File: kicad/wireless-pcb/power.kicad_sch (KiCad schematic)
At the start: 16 parts, among them J2 Conn_01x02_Socket, J4 Conn_01x02_Socket, Q1 AO3401A, U1 XC6206PxxxMR-Regulator_Linear, U8 MCP73832-2-OT

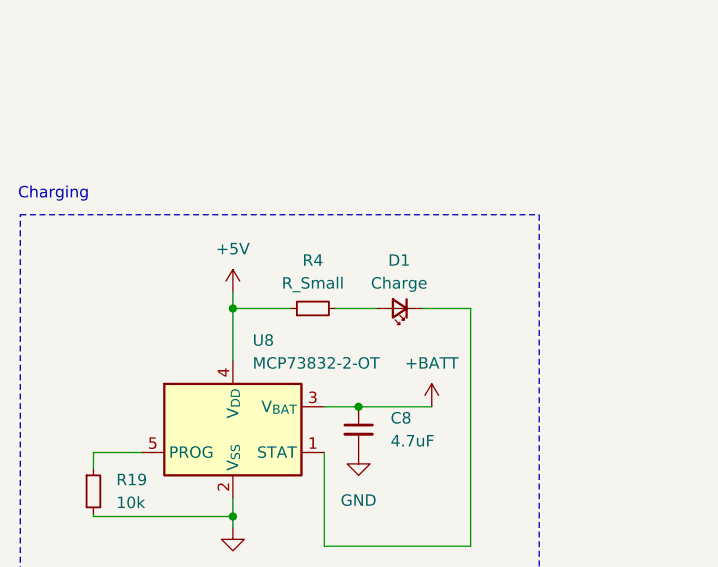
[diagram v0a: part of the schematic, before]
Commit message: Various cleanup, better pin selection, etc.
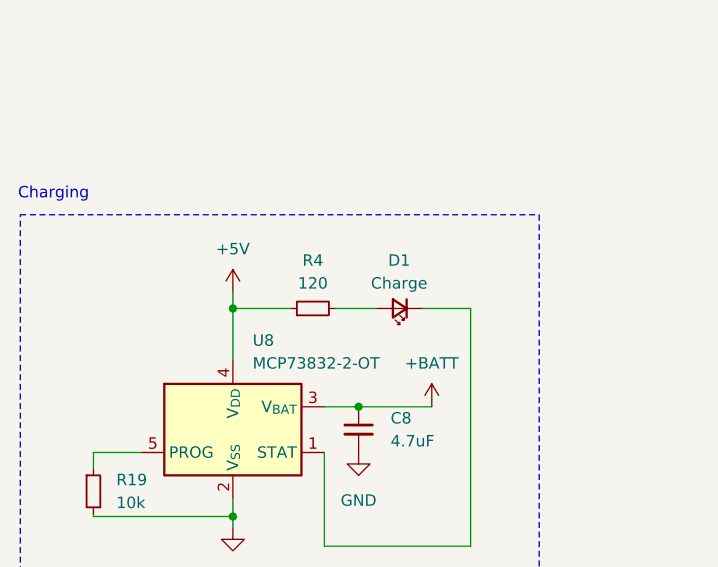
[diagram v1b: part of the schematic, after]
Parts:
- R4: value R_Small -> 120
- R5: LCSC C3016844 -> C3016043
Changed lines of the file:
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@@
       (effects (font (size 1.27 1.27)))
     )
-    (property "Value" "R_Small" (at 74.422 60.96 90)
+    (property "Value" "120" (at 74.422 60.96 90)
       (effects (font (size 1.27 1.27)))
     )
@@
       (effects (font (size 1.27 1.27)) hide)
     )
-    (property "LCSC" "C3016844" (at 221.234 80.01 0)
+    (property "LCSC" "C3016043" (at 221.234 80.01 0)
       (effects (font (size 1.27 1.27)) hide)
     )

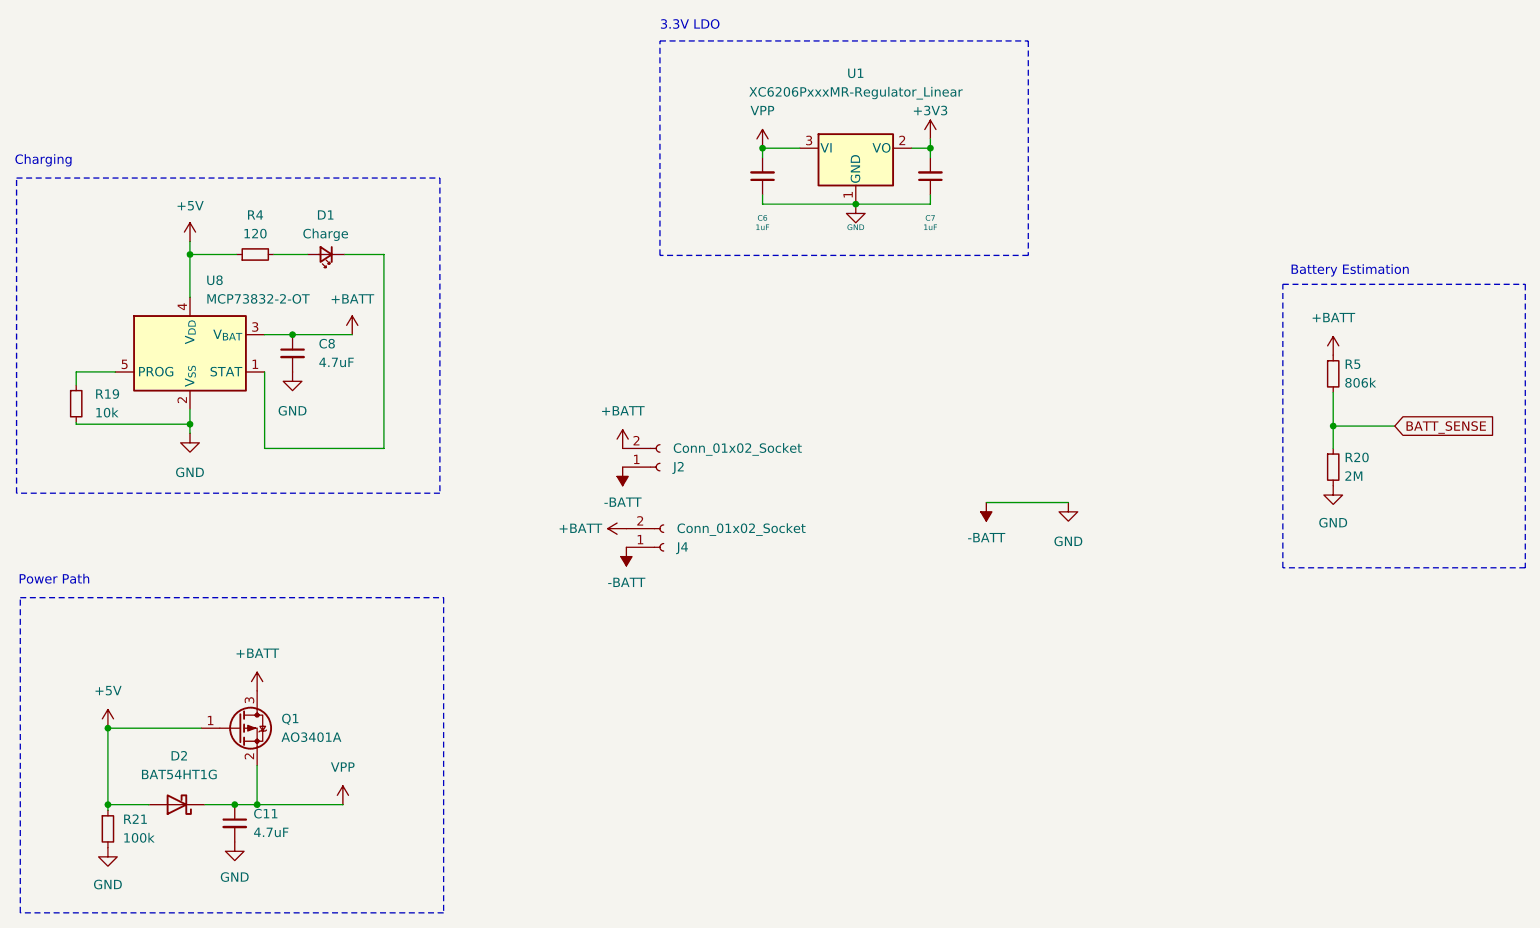
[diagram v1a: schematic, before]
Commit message: BOM tweaks, add some test points, minor placement tweaks.
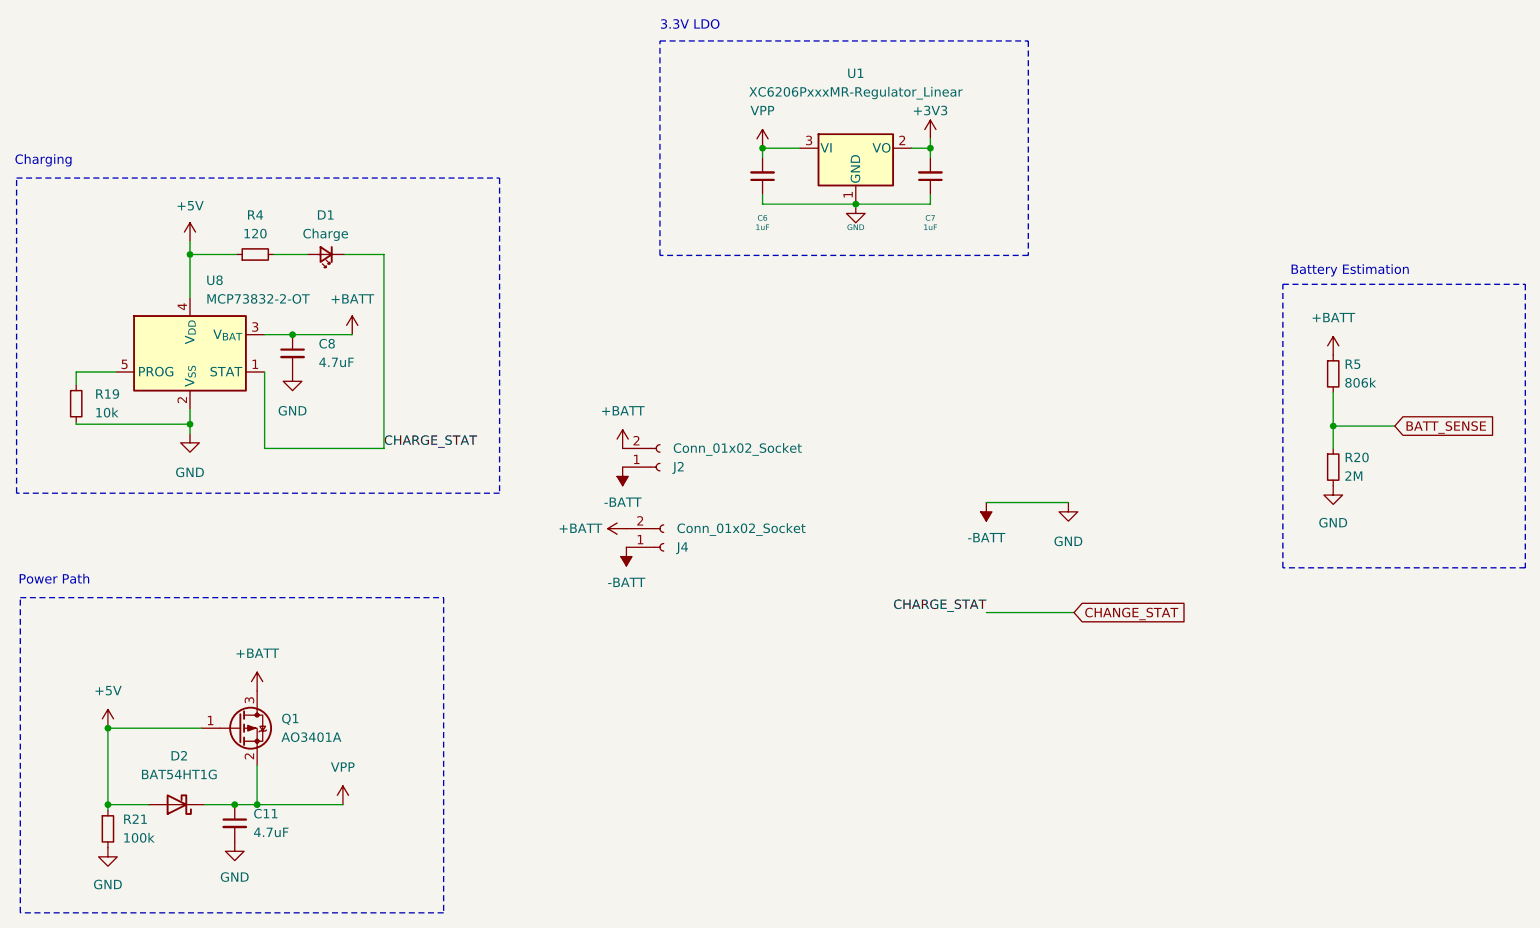
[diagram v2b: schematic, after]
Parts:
- D1: MPN (none) -> Everlight Elec 17-21SURC/S530-A3/4T
- U1: MPN (none) -> XC6206P332MR
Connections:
- net CHANGE_STAT: now reaches D1.1 (K), U8.1 (STAT)
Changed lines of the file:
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@@
+    (stroke (width 0) (type default))
+  )
+  (wire (pts (xy 173.99 112.522) (xy 185.928 112.522))
     (stroke (width 0) (type default))
   )
@@
     (fill (type none))
   )
-  (rectangle (start 41.91 53.34) (end 99.568 96.266)
+  (rectangle (start 41.91 53.34) (end 107.696 96.266)
     (stroke (width 0) (type dot))
     (fill (type none))
@@
   (text "Battery Estimation" (at 215.392 66.802 0)
     (effects (font (size 1.27 1.27)) (justify left bottom))
+  )
+  (label "CHARGE_STAT" (at 91.948 90.17 0) (fields_autoplaced)
+    (effects (font (size 1.27 1.27)) (justify left bottom))
+  )
+  (label "CHARGE_STAT" (at 173.99 112.522 180) (fields_autoplaced)
+    (effects (font (size 1.27 1.27)) (justify right bottom))
+  )
+  (global_label "CHANGE_STAT" (shape input) (at 185.928 112.522 0) (fields_autoplaced)
+    (effects (font (size 1.27 1.27)) (justify left))
+    (property "Intersheetrefs" "${INTERSHEET_REFS}" (at 201.5527 112.522 0)
+      (effects (font (size 1.27 1.27)) (justify left) hide)
+    )
   )
   (global_label "BATT_SENSE" (shape input) (at 229.616 87.122 0) (fields_autoplaced)
@@
       (effects (font (size 1.27 1.27)) hide)
     )
+    (property "MPN" "XC6206P332MR" (at 156.21 49.276 0)
+      (effects (font (size 1.27 1.27)) hide)
+    )
     (pin "1")
     (pin "2")
@@
       (effects (font (size 1.27 1.27)) hide)
     )
+    (property "MPN" "Everlight Elec 17-21SURC/S530-A3/4T " (at 84.074 63.754 0)
+      (effects (font (size 1.27 1.27)) hide)
+    )

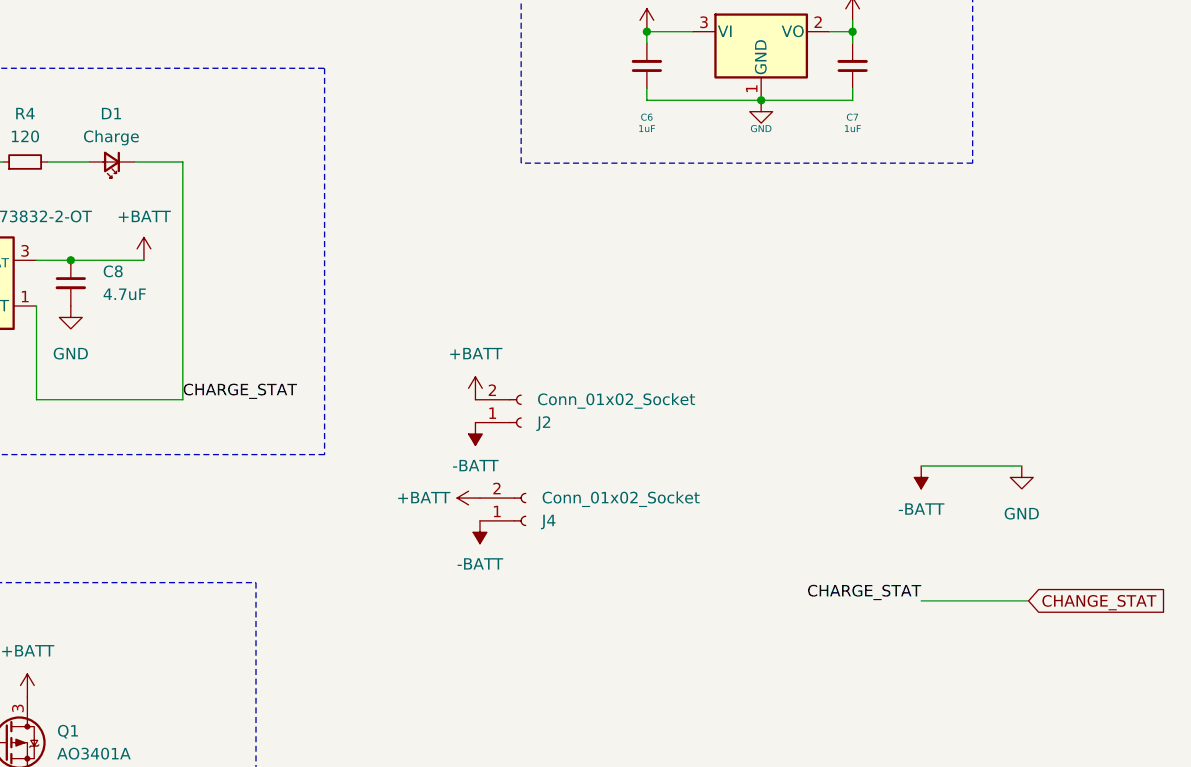
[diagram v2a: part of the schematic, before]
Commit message: Add some jumpers for the charge status bits to be safe.
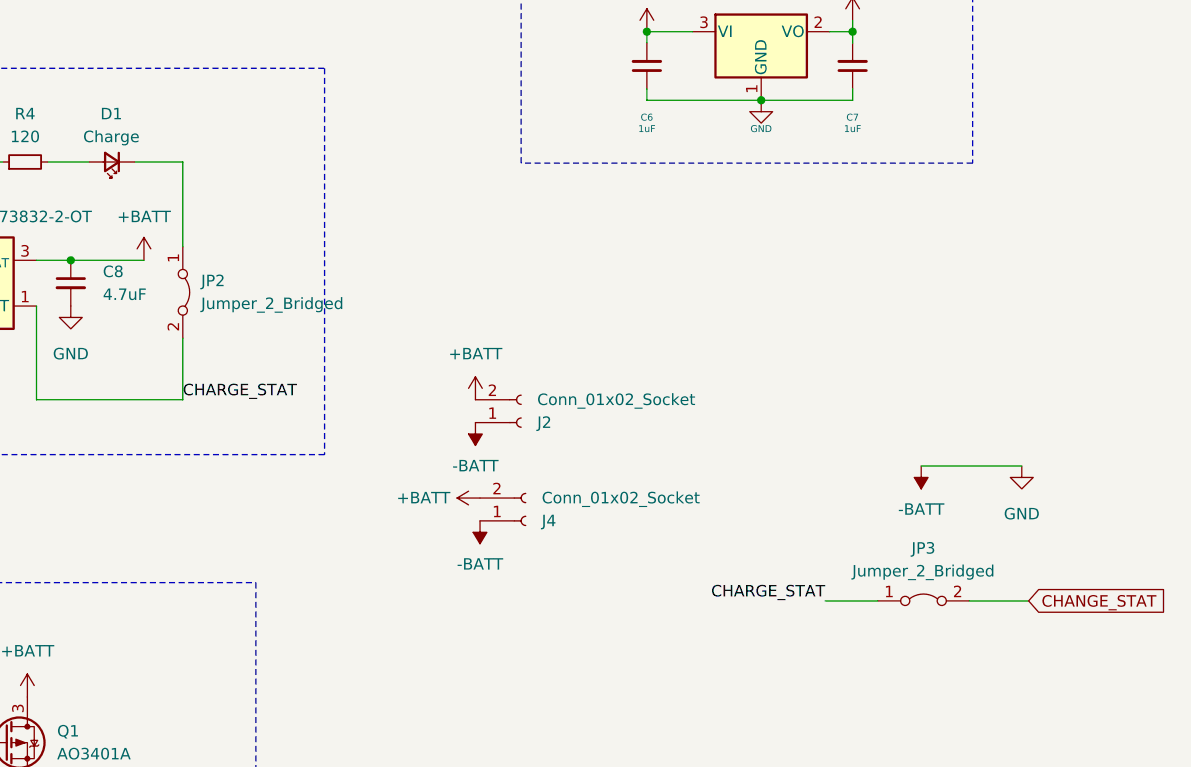
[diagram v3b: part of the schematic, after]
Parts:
- added JP2, JP3: Jumper_2_Bridged, Jumper:SolderJumper-2_P1.3mm_Bridged_RoundedPad1.0x1.5mm, symbol Jumper:Jumper_2_Bridged
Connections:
- net CHANGE_STAT: now also JP3.2 (B); no longer D1.1 (K), U8.1 (STAT)
- new net: D1.1 (K), JP2.1 (A)
- new net CHARGE_STAT: JP2.2 (B), JP3.1 (A), U8.1 (STAT)
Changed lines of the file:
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@@
     (stroke (width 0) (type default))
   )
-  (wire (pts (xy 91.948 90.17) (xy 91.948 63.754))
+  (wire (pts (xy 91.948 90.17) (xy 91.948 83.312))
     (stroke (width 0) (type default))
   )
@@
     (stroke (width 0) (type solid))
   )
+  (wire (pts (xy 179.324 112.522) (xy 185.928 112.522))
+    (stroke (width 0) (type default))
+  )
   (wire (pts (xy 71.628 138.684) (xy 74.676 138.684))
     (stroke (width 0) (type default))
@@
     (stroke (width 0) (type default))
   )
-  (wire (pts (xy 173.99 112.522) (xy 185.928 112.522))
+  (wire (pts (xy 163.322 112.522) (xy 169.164 112.522))
     (stroke (width 0) (type default))
   )
@@
   )
   (wire (pts (xy 65.532 61.976) (xy 65.532 63.754))
+    (stroke (width 0) (type default))
+  )
+  (wire (pts (xy 91.948 73.152) (xy 91.948 63.754))
     (stroke (width 0) (type default))
   )
@@
     (effects (font (size 1.27 1.27)) (justify left bottom))
   )
-  (label "CHARGE_STAT" (at 173.99 112.522 180) (fields_autoplaced)
+  (label "CHARGE_STAT" (at 163.322 112.522 180) (fields_autoplaced)
     (effects (font (size 1.27 1.27)) (justify right bottom))
   )
@@
     )
   )
+  (symbol (lib_id "Jumper:Jumper_2_Bridged") (at 91.948 78.232 270) (unit 1)
+    (in_bom yes) (on_board yes) (dnp no) (fields_autoplaced)
+    (property "Reference" "JP2" (at 93.98 76.962 90)
+      (effects (font (size 1.27 1.27)) (justify left))
+    )
+    (property "Value" "Jumper_2_Bridged" (at 93.98 79.502 90)
+      (effects (font (size 1.27 1.27)) (justify left))
+    )
+    (property "Footprint" "Jumper:SolderJumper-2_P1.3mm_Bridged_RoundedPad1.0x1.5mm" (at 91.948 78.232 0)
+      (effects (font (size 1.27 1.27)) hide)
+    )
+    (property "Datasheet" "~" (at 91.948 78.232 0)
+      (effects (font (size 1.27 1.27)) hide)
+    )
+    (pin "2")
+    (pin "1")
+    (instances
+      (project "le_zapybara"
+        (path "/ca0d59d2-7f9b-4344-99bc-39bc2c8c88cb/75c7772d-c933-4a81-8495-fa59ce9d13a1"
+          (reference "JP2") (unit 1)
+        )
+      )
+    )
+  )
   (symbol (lib_id "power:GND") (at 79.502 79.756 0) (unit 1)
     (in_bom yes) (on_board yes) (dnp no) (fields_autoplaced)
@@
         )
       )
+    )
+  )
+  (symbol (lib_id "Jumper:Jumper_2_Bridged") (at 174.244 112.522 0) (unit 1)
+    (in_bom yes) (on_board yes) (dnp no) (fields_autoplaced)
+    (property "Reference" "JP3" (at 174.244 106.68 0)
+      (effects (font (size 1.27 1.27)))
+    )
+    (property "Value" "Jumper_2_Bridged" (at 174.244 109.22 0)
+      (effects (font (size 1.27 1.27)))
+    )
+    (property "Footprint" "Jumper:SolderJumper-2_P1.3mm_Bridged_RoundedPad1.0x1.5mm" (at 174.244 112.522 0)
+      (effects (font (size 1.27 1.27)) hide)
+    )
+    (property "Datasheet" "~" (at 174.244 112.522 0)
+      (effects (font (size 1.27 1.27)) hide)
+    )
+    (pin "2")
+    (pin "1")
+    (instances
+      (project "le_zapybara"
+        (path "/ca0d59d2-7f9b-4344-99bc-39bc2c8c88cb/75c7772d-c933-4a81-8495-fa59ce9d13a1"
+          (reference "JP3") (unit 1)
+        )
+      )

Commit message: Skip jumpers in the BOM.
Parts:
- JP2, JP3: now left out of the parts list
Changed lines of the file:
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@@
   )
   (symbol (lib_id "Jumper:Jumper_2_Bridged") (at 91.948 78.232 270) (unit 1)
-    (in_bom yes) (on_board yes) (dnp no) (fields_autoplaced)
+    (in_bom no) (on_board yes) (dnp no) (fields_autoplaced)
     (property "Reference" "JP2" (at 93.98 76.962 90)
       (effects (font (size 1.27 1.27)) (justify left))
@@
   )
   (symbol (lib_id "Jumper:Jumper_2_Bridged") (at 174.244 112.522 0) (unit 1)
-    (in_bom yes) (on_board yes) (dnp no) (fields_autoplaced)
+    (in_bom no) (on_board yes) (dnp no) (fields_autoplaced)
     (property "Reference" "JP3" (at 174.244 106.68 0)
       (effects (font (size 1.27 1.27)))
